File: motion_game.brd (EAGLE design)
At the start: 127 x 68.2 mm, 29 parts, among them U1 MOD-LED8X8RGB-CONN, U2 MOD-LED8X8RGB-CONN, U3 POCKETBEAGLE

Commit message: add gerber files
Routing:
- net GND: track 329.1 -> 86.4 mm
- net SYS_VDD1_3P3V: track 52.5 -> 60.9 mm
- net BTN3: track 92.9 -> 89.4 mm, vias 0 -> 2
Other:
- board text added: "0.1uF"
- board text added: "10nF"
- board text added: "ENGI 301 Maze Game Irene Zhang zz36"

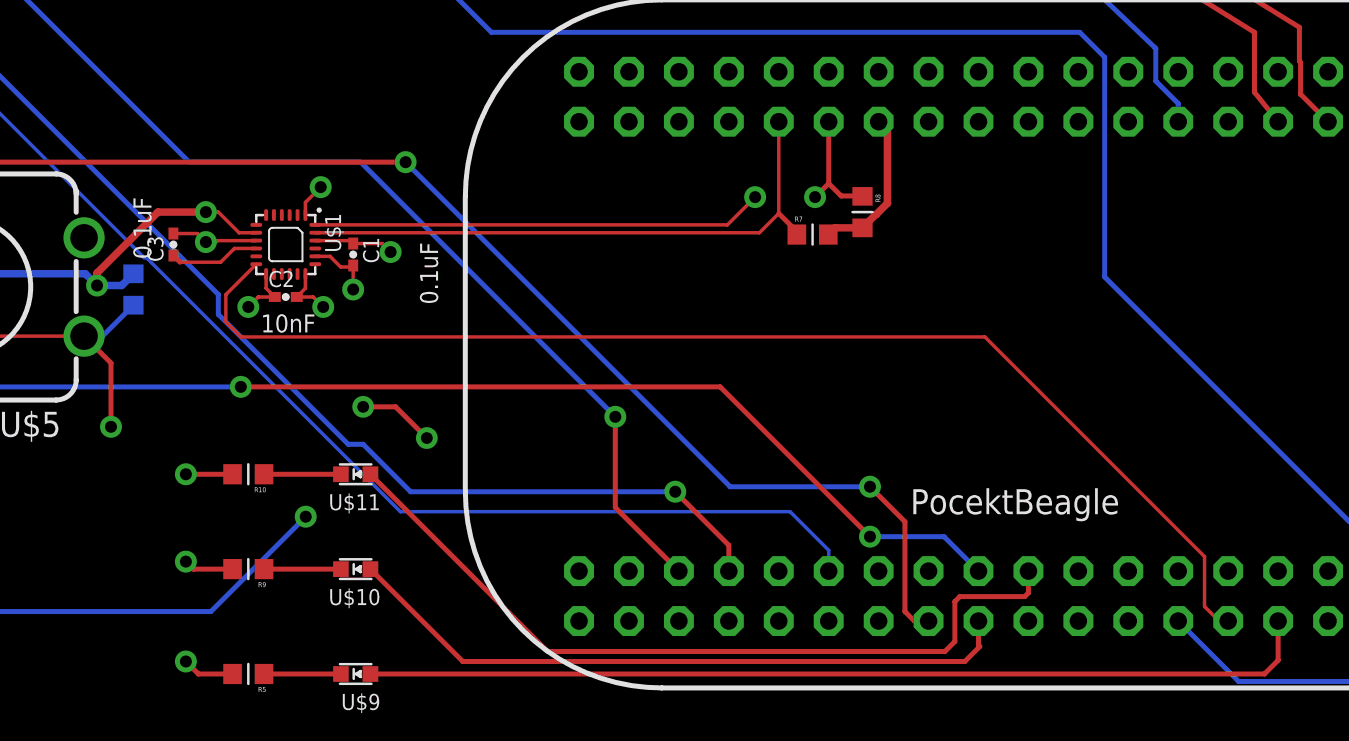
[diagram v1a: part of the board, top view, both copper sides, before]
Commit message: adjust Vdd
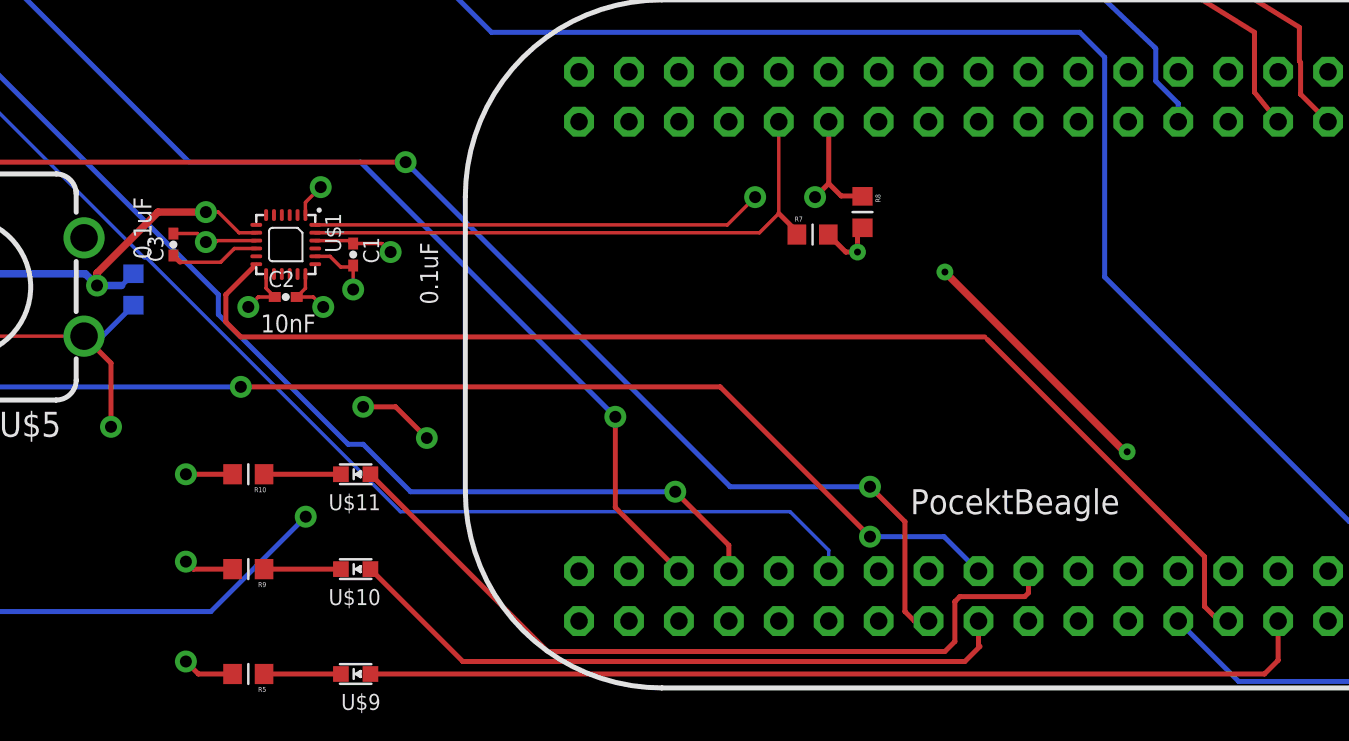
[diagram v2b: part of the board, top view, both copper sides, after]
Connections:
- removed net SYS_VDD1_3P3V: C1.1, C2.1, R0.2, R1.2, R2.2, R3.2, R4.2, R7.2, R8.2, U$1.P$1, U$1.P$13, U$1.P$22, U$1.P$8, U1.1, U2.1, U3.14, U3.24, U3.49, U3.59
- new net VDD_3V: C1.1, C2.1, R0.2, R1.2, R2.2, R3.2, R4.2, R7.2, R8.2, U$1.P$1, U$1.P$13, U$1.P$22, U$1.P$8, U3.14, U3.59
- new net VDD_5V: U1.1, U2.1, U3.24, U3.49
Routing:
- net VDD_5V: track 0.00 -> 122.2 mm, vias 0 -> 2
- net SYS_VDD1_3P3V: track 60.9 -> 0.00 mm, vias 9 -> 0
- net VDD_3V: track 0.00 -> 51.2 mm, vias 0 -> 10
- added copper zone on layer 2, net VDD_3V
- removed copper zone on layer 2, net SYS_VDD1_3P3V
